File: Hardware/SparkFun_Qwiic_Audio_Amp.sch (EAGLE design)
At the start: 46 parts, among them J1 QWIIC, J2 TRS_INPUT, J6 SCREW, U6 TPA2016D2RTJ

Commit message: Layout done v01
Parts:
- added C17, C4: 0.1uF, SparkFun-Capacitors:0.1UF-0402T-16V-10%-X7R-WE
- added C2: 10uF, SparkFun-Capacitors:10UF-0805-25V-10%
- added JP1: JP1, SparkFun-Jumpers:JUMPER-SMT_2_NO_SILK
- added LOGO6: SPECIAL_INSTRUCTIONS-ORDERING, SparkFun-Aesthetics:SPECIAL_INSTRUCTIONS-ORDERING
- added TP1, TP2: TEST-POINTTP_15TH_THRU, SparkFun-Connectors:TEST-POINTTP_15TH_THRU
- C10, C11, C12, C9: device SparkFun-Passives:CAP0402-CAP -> SparkFun-Capacitors:1.0NF/1000PF-0402-25V-10%-X7R
- C13, C15: value 10uF -> 1.0uF; device SparkFun:CAP_POL1206 -> SparkFun-Capacitors:1.0UF-0402T-16V-10%
- C14, C16: device SparkFun:CAP0402-CAP -> SparkFun-Capacitors:0.1UF-0402T-16V-10%-X7R-WE
- C5: value 1uF -> 1.0uF; device SparkFun:CAP0603-CAP -> SparkFun-Capacitors:1.0UF-0402T-16V-10%
- C6, C7, C8: value 1uF -> 1.0uF; device SparkFun:CAP0402-CAP -> SparkFun-Capacitors:1.0UF-0402T-16V-10%
- J4: device SparkFun-Connectors:CONN_022.54MM_SCREWTERM -> SparkFun-Connectors:CONN_023.5MM
- L1, L2, L3, L4: value (none) -> 220Ω; device SparkFun-Passives:INDUCTOR0805 -> SparkFun-Coils:FERRITE_BEAD-0805-220Ω-100MHZ-2A
- R1: value 10k -> 100k; device SparkFun-Resistors:10KOHM-0402T-1/16W-1% -> SparkFun-Resistors:100KOHM-0402T-1/16W-1%
- R2, R3: value 4.7k -> 2.2k; device SparkFun-Resistors:4.7KOHM-0402T-1/16W-1% -> SparkFun-Resistors:2.2KOHM-0402T-1/16W-1%
- U6: value TPA2016D2RTJ -> TPA2016D2; device mike-temp:TPA2016D2RTJ -> temp:TPA2016D2RTJ
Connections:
- net SPKL+ renamed SPK_R_+
- net SPKL- renamed SPK_R_-
- net SPKR+ renamed SPK_L_+
- net SPKR- renamed SPK_L_-
- net 3.3V: now also JP1.1
- net GND: now also C13.2, C15.2, C17.2, C2.2, C4.2; no longer C13.-, C15.-
- net SCL: now also TP1.1
- net SDA: now also TP2.1
- net SDZ: now also C4.1
- net VCC: now also C13.1, C15.1, C17.1, C2.1, JP1.2; no longer C13.+, C15.+
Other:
- note added: "Close this jumper to power from qwiic. Only use if doing low power output."
- note added: "I2C Address: 0x58 (unshifted) I2C write: 0xB0 I2C read: 0xB1"
- note added: "With nothing plugged into J2, Screw Terminal INPUTs (J6) pass through J2. With audio cable inserted into J2, then TRS cable replaces signals."
- note removed: "With nothing plugged into J2, Screwpin INPUTs (J3) pass through J2. With audio cable inserted into J2, then audio cable replaces signals."
- moved on the sheet: C1, C14, C16, C3, C5, C6, C7, C8, I2C, J1, J2, J4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

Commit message: swapped inner layers to correct (2=GND, 15=VCC)
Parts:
- LOGO6: PROD_ID (none) -> PCB-17002
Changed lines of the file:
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@@
 <grid distance="0.1" unitdist="inch" unit="inch" style="lines" multiple="1" display="no" altdistance="0.01" altunitdist="inch" altunit="inch"/>
 <layers>
-<layer number="1" name="Top" color="4" fill="1" visible="yes" active="no"/>
-<layer number="2" name="Route2" color="6" fill="5" visible="yes" active="no"/>
-<layer number="3" name="Route3" color="17" fill="1" visible="yes" active="no"/>
-<layer number="4" name="Route4" color="18" fill="1" visible="yes" active="no"/>
-<layer number="5" name="Route5" color="19" fill="1" visible="yes" active="no"/>
-<layer number="6" name="Route6" color="25" fill="1" visible="yes" active="no"/>
-<layer number="7" name="Route7" color="26" fill="1" visible="yes" active="no"/>
-<layer number="8" name="Route8" color="27" fill="1" visible="yes" active="no"/>
-<layer number="9" name="Route9" color="28" fill="1" visible="yes" active="no"/>
-<layer number="10" name="Route10" color="29" fill="1" visible="yes" active="no"/>
-<layer number="11" name="Route11" color="30" fill="1" visible="yes" active="no"/>
-<layer number="12" name="Route12" color="20" fill="1" visible="yes" active="no"/>
-<layer number="13" name="Route13" color="21" fill="1" visible="yes" active="no"/>
-<layer number="14" name="Route14" color="22" fill="1" visible="yes" active="no"/>
-<layer number="15" name="Route15" color="23" fill="3" visible="yes" active="no"/>
-<layer number="16" name="Bottom" color="1" fill="1" visible="yes" active="no"/>
-<layer number="17" name="Pads" color="2" fill="1" visible="yes" active="no"/>
-<layer number="18" name="Vias" color="2" fill="1" visible="yes" active="no"/>
-<layer number="19" name="Unrouted" color="6" fill="1" visible="yes" active="no"/>
-<layer number="20" name="Dimension" color="24" fill="1" visible="yes" active="no"/>
-<layer number="21" name="tPlace" color="16" fill="1" visible="yes" active="no"/>
-<layer number="22" name="bPlace" color="14" fill="1" visible="yes" active="no"/>
-<layer number="23" name="tOrigins" color="15" fill="1" visible="yes" active="no"/>
-<layer number="24" name="bOrigins" color="15" fill="1" visible="yes" active="no"/>
-<layer number="25" name="tNames" color="7" fill="1" visible="yes" active="no"/>
-<layer number="26" name="bNames" color="7" fill="1" visible="yes" active="no"/>
-<layer number="27" name="tValues" color="7" fill="1" visible="yes" active="no"/>
-<layer number="28" name="bValues" color="7" fill="1" visible="yes" active="no"/>
+<layer number="1" name="Top" color="4" fill="1" visible="no" active="no"/>
+<layer number="2" name="Route2" color="6" fill="5" visible="no" active="no"/>
+<layer number="3" name="Route3" color="17" fill="1" visible="no" active="no"/>
+<layer number="4" name="Route4" color="18" fill="1" visible="no" active="no"/>
+<layer number="5" name="Route5" color="19" fill="1" visible="no" active="no"/>
+<layer number="6" name="Route6" color="25" fill="1" visible="no" active="no"/>
+<layer number="7" name="Route7" color="26" fill="1" visible="no" active="no"/>
+<layer number="8" name="Route8" color="27" fill="1" visible="no" active="no"/>
+<layer number="9" name="Route9" color="28" fill="1" visible="no" active="no"/>
+<layer number="10" name="Route10" color="29" fill="1" visible="no" active="no"/>
+<layer number="11" name="Route11" color="30" fill="1" visible="no" active="no"/>
+<layer number="12" name="Route12" color="20" fill="1" visible="no" active="no"/>
+<layer number="13" name="Route13" color="21" fill="1" visible="no" active="no"/>
+<layer number="14" name="Route14" color="22" fill="1" visible="no" active="no"/>
+<layer number="15" name="Route15" color="23" fill="3" visible="no" active="no"/>
+<layer number="16" name="Bottom" color="1" fill="1" visible="no" active="no"/>
+<layer number="17" name="Pads" color="2" fill="1" visible="no" active="no"/>
+<layer number="18" name="Vias" color="2" fill="1" visible="no" active="no"/>
+<layer number="19" name="Unrouted" color="6" fill="1" visible="no" active="no"/>
+<layer number="20" name="Dimension" color="24" fill="1" visible="no" active="no"/>
+<layer number="21" name="tPlace" color="16" fill="1" visible="no" active="no"/>
+<layer number="22" name="bPlace" color="14" fill="1" visible="no" active="no"/>
+<layer number="23" name="tOrigins" color="15" fill="1" visible="no" active="no"/>
+<layer number="24" name="bOrigins" color="15" fill="1" visible="no" active="no"/>
+<layer number="25" name="tNames" color="7" fill="1" visible="no" active="no"/>
+<layer number="26" name="bNames" color="7" fill="1" visible="no" active="no"/>
+<layer number="27" name="tValues" color="7" fill="1" visible="no" active="no"/>
+<layer number="28" name="bValues" color="7" fill="1" visible="no" active="no"/>
 <layer number="29" name="tStop" color="7" fill="3" visible="no" active="no"/>
 <layer number="30" name="bStop" color="7" fill="6" visible="no" active="no"/>
@@
 <layer number="35" name="tGlue" color="7" fill="4" visible="no" active="no"/>
 <layer number="36" name="bGlue" color="7" fill="5" visible="no" active="no"/>
-<layer number="37" name="tTest" color="7" fill="1" visible="yes" active="no"/>
-<layer number="38" name="bTest" color="7" fill="1" visible="yes" active="no"/>
+<layer number="37" name="tTest" color="7" fill="1" visible="no" active="no"/>
+<layer number="38" name="bTest" color="7" fill="1" visible="no" active="no"/>
 <layer number="39" name="tKeepout" color="4" fill="11" visible="no" active="no"/>
 <layer number="40" name="bKeepout" color="1" fill="11" visible="no" active="no"/>
@@
 <layer number="44" name="Drills" color="7" fill="1" visible="no" active="no"/>
 <layer number="45" name="Holes" color="7" fill="1" visible="no" active="no"/>
-<layer number="46" name="Milling" color="3" fill="1" visible="yes" active="no"/>
-<layer number="47" name="Measures" color="7" fill="1" visible="yes" active="no"/>
-<layer number="48" name="Document" color="7" fill="1" visible="yes" active="no"/>
-<layer number="49" name="Reference" color="13" fill="1" visible="yes" active="no"/>
-<layer number="50" name="dxf" color="7" fill="1" visible="yes" active="no"/>
-<layer number="51" name="tDocu" color="6" fill="1" visible="yes" active="no"/>
-<layer number="52" name="bDocu" color="7" fill="1" visible="yes" active="no"/>
-<layer number="53" name="tGND_GNDA" color="7" fill="9" visible="yes" active="no"/>
-<layer number="54" name="bGND_GNDA" color="1" fill="9" visible="yes" active="no"/>
-<layer number="56" name="wert" color="7" fill="1" visible="yes" active="no"/>
-<layer number="57" name="tCAD" color="7" fill="1" visible="yes" active="no"/>
-<layer number="58" name="bCAD" color="7" fill="1" visible="yes" active="no"/>
-<layer number="59" name="tCarbon" color="7" fill="1" visible="yes" active="no"/>
-<layer number="60" name="bCarbon" color="7" fill="1" visible="yes" active="no"/>
+<layer number="46" name="Milling" color="3" fill="1" visible="no" active="no"/>
+<layer number="47" name="Measures" color="7" fill="1" visible="no" active="no"/>
+<layer number="48" name="Document" color="7" fill="1" visible="no" active="no"/>
+<layer number="49" name="Reference" color="13" fill="1" visible="no" active="no"/>
+<layer number="50" name="dxf" color="7" fill="1" visible="no" active="no"/>
+<layer number="51" name="tDocu" color="6" fill="1" visible="no" active="no"/>
+<layer number="52" name="bDocu" color="7" fill="1" visible="no" active="no"/>
+<layer number="53" name="tGND_GNDA" color="7" fill="9" visible="no" active="no"/>
+<layer number="54" name="bGND_GNDA" color="1" fill="9" visible="no" active="no"/>
+<layer number="56" name="wert" color="7" fill="1" visible="no" active="no"/>
+<layer number="57" name="tCAD" color="7" fill="1" visible="no" active="no"/>
+<layer number="58" name="bCAD" color="7" fill="1" visible="no" active="no"/>
+<layer number="59" name="tCarbon" color="7" fill="1" visible="no" active="no"/>
+<layer number="60" name="bCarbon" color="7" fill="1" visible="no" active="no"/>
 <layer number="88" name="SimResults" color="9" fill="1" visible="yes" active="yes"/>
 <layer number="89" name="SimProbes" color="9" fill="1" visible="yes" active="yes"/>
@@
 <part name="JP1" library="SparkFun-Jumpers" deviceset="JUMPER-SMT_2_NO" device="_SILK" package3d_urn="urn:adsk.eagle:package:39279/1" value="JP1"/>
 <part name="SUPPLY12" library="SparkFun-PowerSymbols" deviceset="VCC" device=""/>
-<part name="LOGO6" library="SparkFun-Aesthetics" deviceset="SPECIAL_INSTRUCTIONS" device="-ORDERING"/>
+<part name="LOGO6" library="SparkFun-Aesthetics" deviceset="SPECIAL_INSTRUCTIONS" device="-ORDERING">
+<attribute name="PROD_ID" value="PCB-17002"/>
+</part>
 <part name="TP1" library="SparkFun-Connectors" deviceset="TEST-POINT" device="TP_15TH_THRU" value=""/>
 <part name="TP2" library="SparkFun-Connectors" deviceset="TEST-POINT" device="TP_15TH_THRU" value=""/>
@@
 <attribute name="VALUE" x="114.3" y="51.054" size="1.778" layer="96" font="vector" rot="MR0" align="bottom-center"/>
 </instance>
-<instance part="LOGO6" gate="G$1" x="226.06" y="22.86" smashed="yes"/>
+<instance part="LOGO6" gate="G$1" x="226.06" y="22.86" smashed="yes">
+<attribute name="PROD_ID" x="226.06" y="22.86" size="1.27" layer="96" display="off"/>
+</instance>
 <instance part="TP1" gate="G$1" x="76.2" y="12.7" smashed="yes" rot="R180">
 <attribute name="NAME" x="75.438" y="15.748" size="1.778" layer="95" font="vector" rot="R180"/>

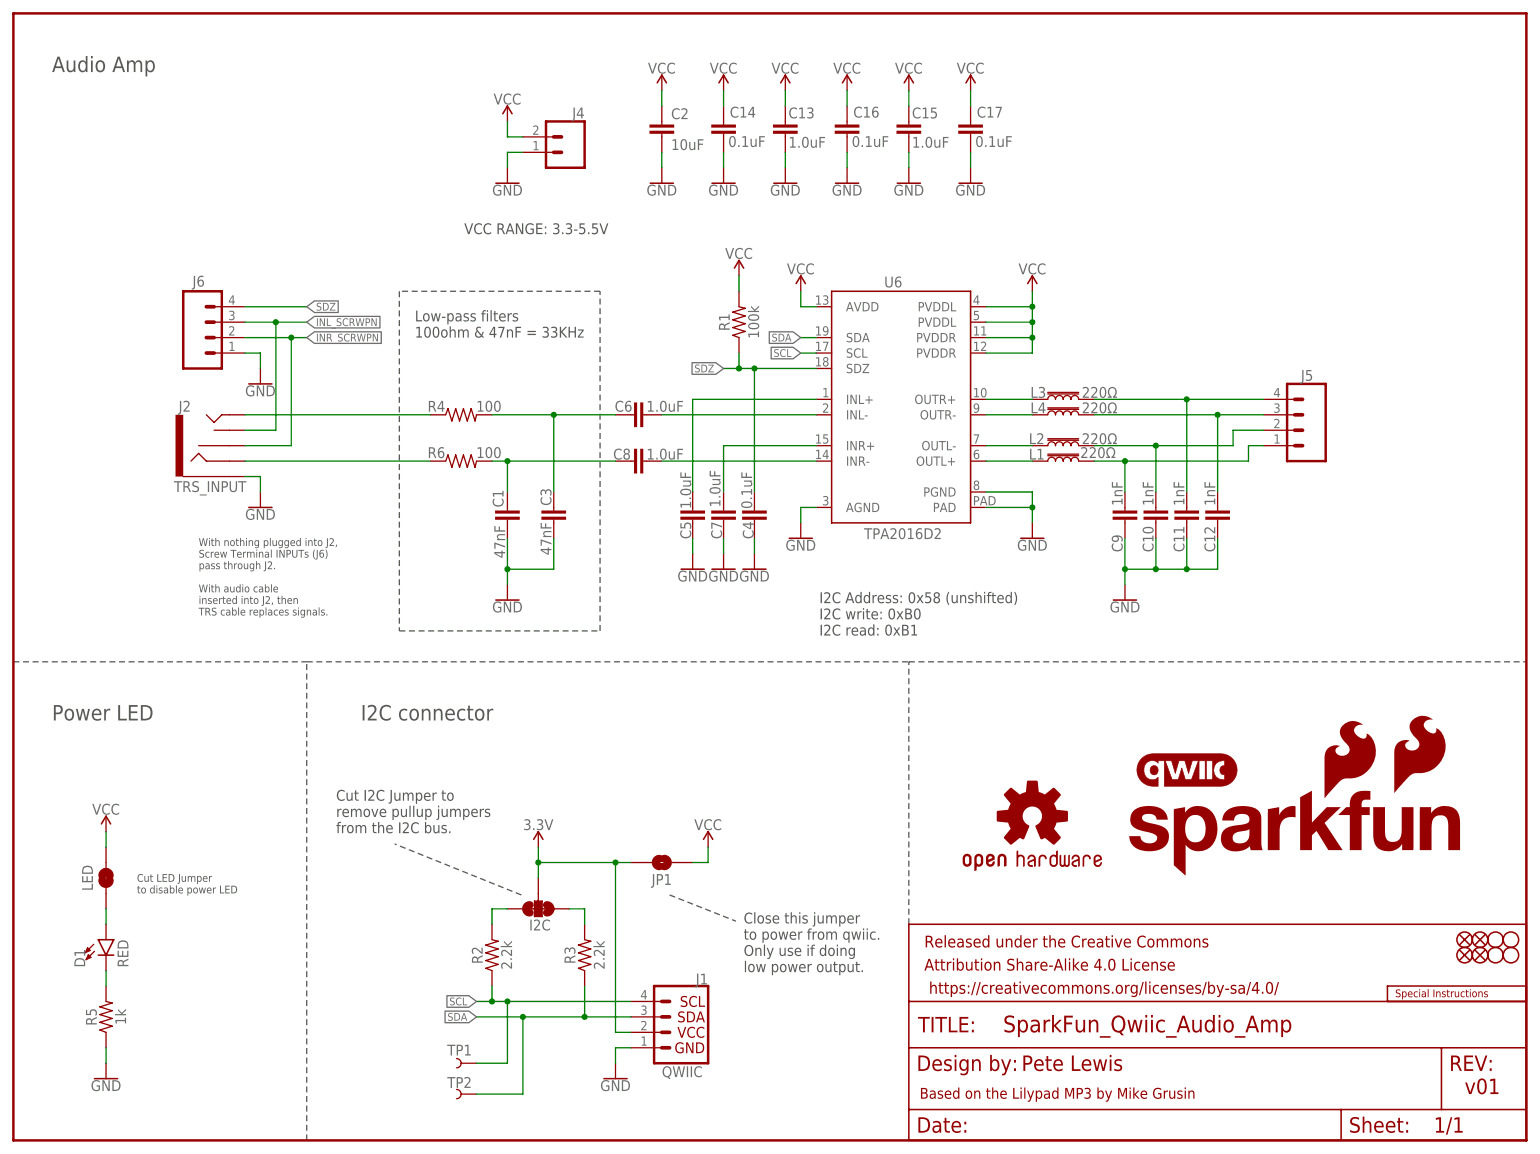
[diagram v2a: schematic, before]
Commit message: schematic cleanup and minor board fixes
-more gnd vias
-drc approvals
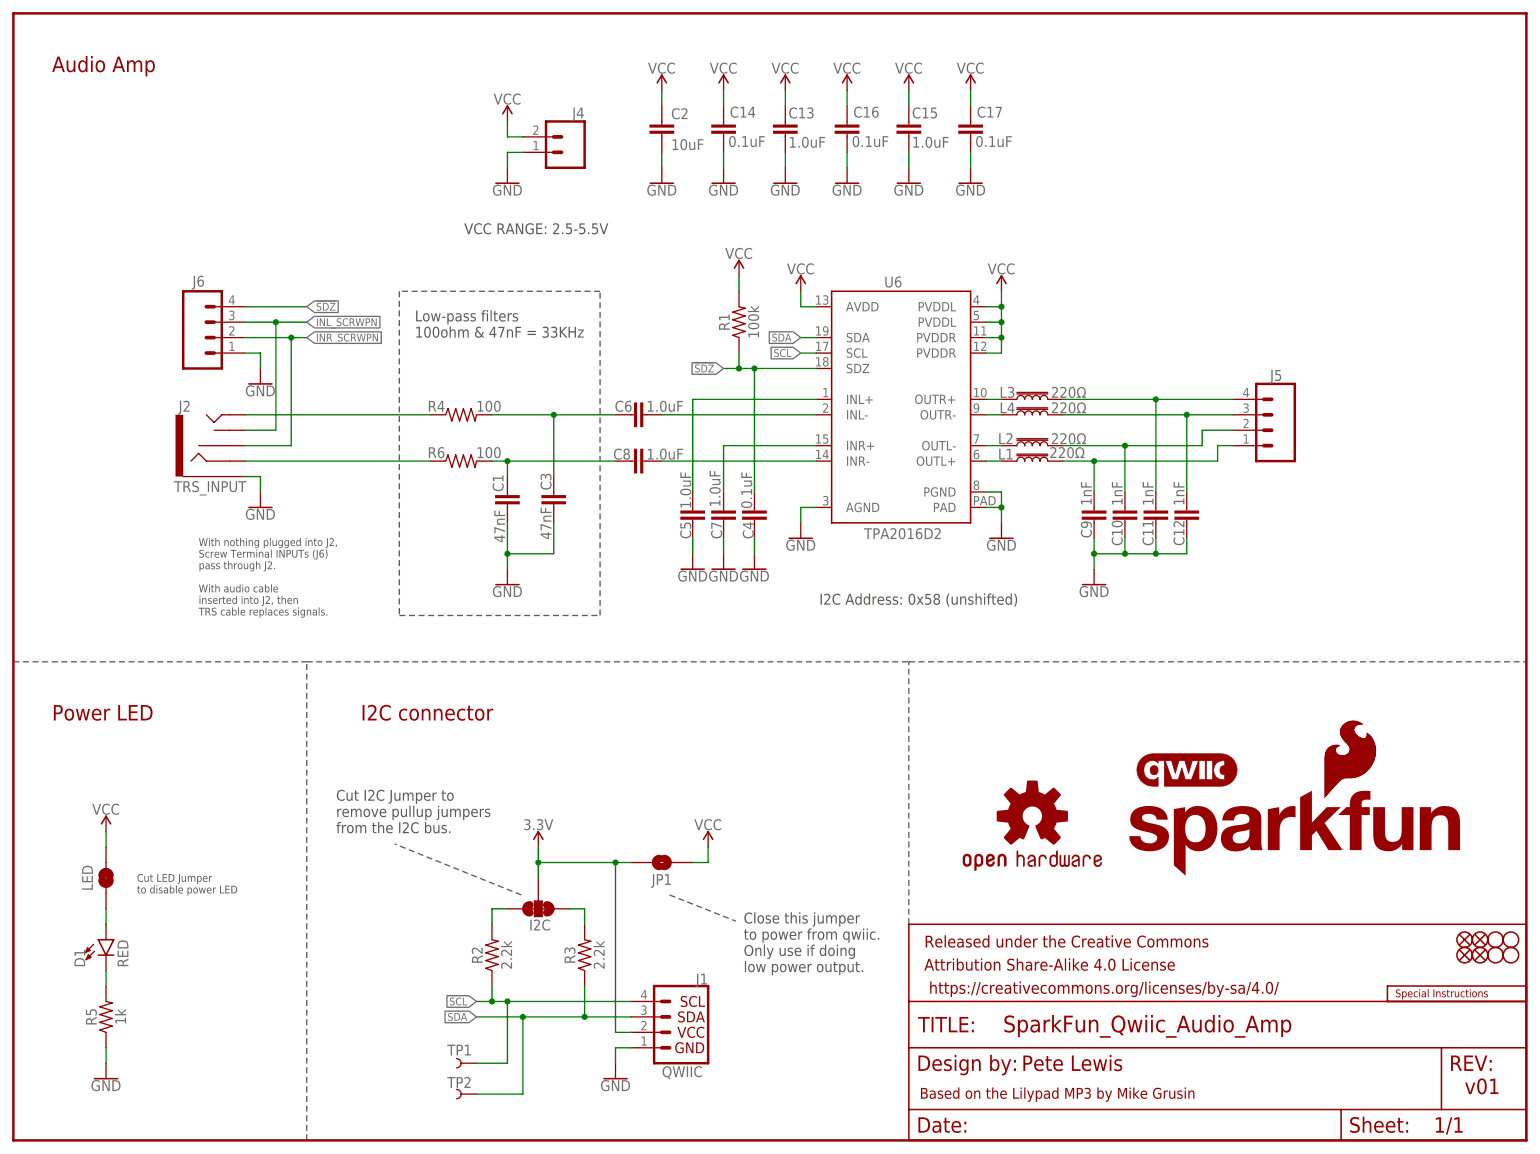
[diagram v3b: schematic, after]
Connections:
- net SDZ renamed !SDZ!
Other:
- note added: "I2C Address: 0x58 (unshifted)"
- note added: "VCC RANGE: 2.5-5.5V"
- note removed: "I2C Address: 0x58 (unshifted) I2C write: 0xB0 I2C read: 0xB1"
- note removed: "VCC RANGE: 3.3-5.5V"
- moved on the sheet: C1, C10, C11, C12, C3, C9, J5, L1, L2, L3, L4
